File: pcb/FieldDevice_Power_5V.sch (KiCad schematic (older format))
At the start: 17 parts

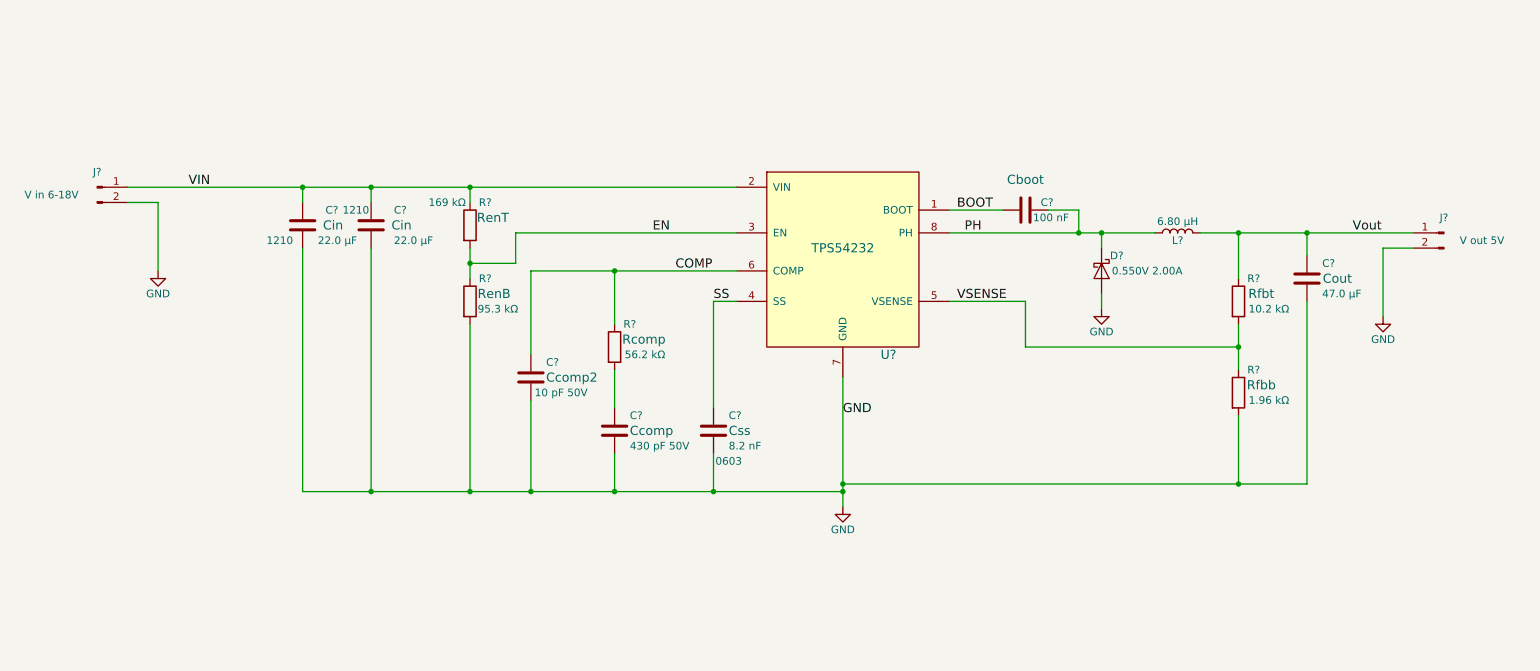
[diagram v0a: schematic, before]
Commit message: Completed the schematic and started the layout
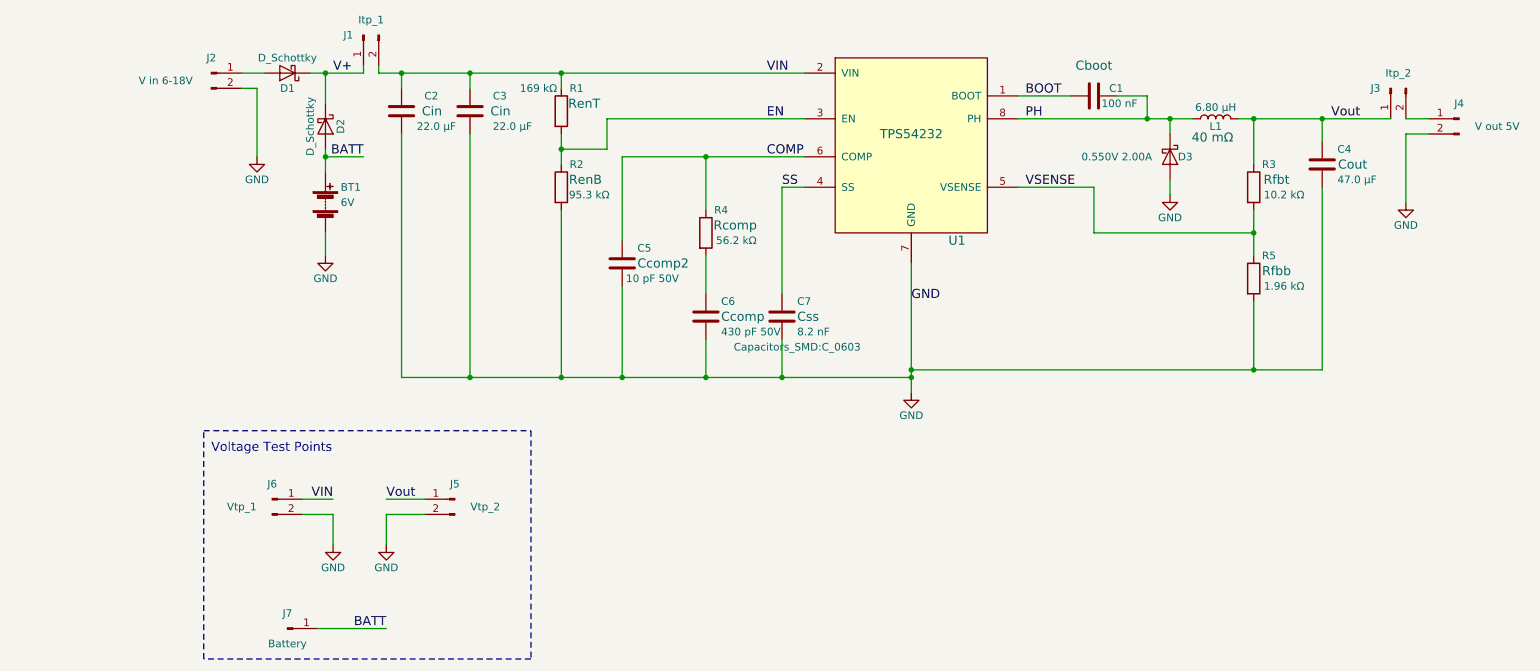
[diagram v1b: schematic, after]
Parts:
- added BT1: 6V, FieldDevice_Power_5V:BC4AAAPC_BATTERYHOLDER_4xAAA, symbol Battery
- added D1: D_Schottky, FieldDevice_Power_5V:B130-13-F, symbol D_Schottky
- added D2: D_Schottky, Diodes_SMD:D_SOD-123F, symbol D_Schottky
- added J1: Itp_1, Pin_Headers:Pin_Header_Straight_1x02_Pitch2.54mm, symbol Conn_01x02_Male
- added J3: Itp_2, Pin_Headers:Pin_Header_Straight_1x02_Pitch2.54mm, symbol Conn_01x02_Male
- added J5: Vtp_2, Pin_Headers:Pin_Header_Straight_1x02_Pitch2.54mm, symbol Conn_01x02_Male
- added J6: Vtp_1, Pin_Headers:Pin_Header_Straight_1x02_Pitch2.54mm, symbol Conn_01x02_Male
- added J7: Battery, Pin_Headers:Pin_Header_Straight_1x01, symbol Conn_01x01_Male
- C1, C4, C5, C6: renamed from C?; footprint (none) -> Capacitors_SMD:C_0805
- C2, C3: renamed from C?; footprint 1210 -> Capacitors_SMD:C_1210; ConradPN (none) -> Value; Label (none) -> Value; MPN (none) -> Value
- C7: renamed from C?; footprint 0603 -> Capacitors_SMD:C_0603
- D3: renamed from D?; footprint SOD-123F -> Diodes_SMD:D_SOD-123F; ConradPN (none) -> Value; Label (none) -> Value; MPN (none) -> SS24FL
- J2, J4: renamed from J?; footprint (none) -> Pin_Headers:Pin_Header_Straight_1x02_Pitch2.54mm
- L1: renamed from L?; footprint (none) -> FieldDevice_Power_5V:SDR0805-6R8ML; Comp_Name Value -> 40 mΩ; ConradPN (none) -> Value; Label (none) -> Value; MPN (none) -> Value
- R1, R2, R3, R4, R5: renamed from R?; footprint (none) -> Resistors_SMD:R_0805
- U1: renamed from U?; footprint (none) -> FieldDevice_Power_5V:TPS54232DR
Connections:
- net GND: now also BT1.2 (-), J5.2 (Pin_2), J6.2 (Pin_2)
- net VIN: now also J1.2 (Pin_2), J6.1 (Pin_1); no longer J2.1 (Pin_1)
- net Vout: now also J3.1 (Pin_1), J5.1 (Pin_1); no longer J4.1 (Pin_1)
- new net: J3.2 (Pin_2), J4.1 (Pin_1)
- new net: D1.2 (A), J2.1 (Pin_1)
- new net BATT: BT1.1 (+), D2.2 (A), J7.1 (Pin_1)
- new net V+: D1.1 (K), D2.1 (K), J1.1 (Pin_1)
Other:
- note added: "Voltage Test Points"
- moved on the sheet: C1, C2, C3, C4, C5, C6, C7, D3, J2, J4, L1, R1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

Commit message: More on the layout
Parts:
- D1: value D_Schottky -> B130-13-F
- D2: value D_Schottky -> B130-13-F; footprint Diodes_SMD:D_SOD-123F -> FieldDevice_Power_5V:B130-13-F
- D3: footprint Diodes_SMD:D_SOD-123F -> FieldDevice_Power_5V:D_SOD-123F
- J1, J2, J3, J4, J5, J6: footprint Pin_Headers:Pin_Header_Straight_1x02_Pitch2.54mm -> Pin_Headers:Pin_Header_Angled_1x02_Pitch2.54mm
- J7: footprint Pin_Headers:Pin_Header_Straight_1x01 -> Pin_Headers:Pin_Header_Angled_1x01
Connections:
- net GND: now also J6.1 (Pin_1); no longer J6.2 (Pin_2)
- net VIN: now also J6.2 (Pin_2); no longer J6.1 (Pin_1)
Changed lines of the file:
@@
 F 0 "D3" V 8250 2650 50  0000 C CNN
 F 1 "0.550V 2.00A" V 8250 2200 50  0000 C CNN
-F 2 "Diodes_SMD:D_SOD-123F" H 8250 2550 50  0001 C CNN
+F 2 "FieldDevice_Power_5V:D_SOD-123F" H 8250 2550 50  0001 C CNN
 F 3 "https://www.fairchildsemi.com/datasheets/SS/SS24FL.pdf" H 8250 2550 50  0001 C CNN
 F 4 "SS24FL" H 8250 2550 60  0001 C CNN "MPN"
@@
 F 0 "J4" H 10150 2400 50  0000 C CNN
 F 1 "V out 5V" H 9900 2250 50  0000 C CNN
-F 2 "Pin_Headers:Pin_Header_Straight_1x02_Pitch2.54mm" H 10150 2300 50  0001 C CNN
+F 2 "Pin_Headers:Pin_Header_Angled_1x02_Pitch2.54mm" H 10150 2300 50  0001 C CNN
 F 3 "" H 10150 2300 50  0001 C CNN
 F 4 "Value" H 10150 2300 60  0001 C CNN "Link"
@@
 F 0 "J2" H 1950 2100 50  0000 C CNN
 F 1 "V in 6-18V" H 1650 1950 50  0000 C CNN
-F 2 "Pin_Headers:Pin_Header_Straight_1x02_Pitch2.54mm" H 1950 2000 50  0001 C CNN
+F 2 "Pin_Headers:Pin_Header_Angled_1x02_Pitch2.54mm" H 1950 2000 50  0001 C CNN
 F 3 "" H 1950 2000 50  0001 C CNN
 F 4 "Value" H 1950 2000 60  0001 C CNN "Link"
@@
 F 0 "J1" V 2950 1850 50  0000 C CNN
 F 1 "Itp_1" V 2850 1700 50  0000 C CNN
-F 2 "Pin_Headers:Pin_Header_Straight_1x02_Pitch2.54mm" H 2950 1750 50  0001 C CNN
+F 2 "Pin_Headers:Pin_Header_Angled_1x02_Pitch2.54mm" H 2950 1750 50  0001 C CNN
 F 3 "" H 2950 1750 50  0001 C CNN
 F 4 "Value" H 2950 1750 60  0001 C CNN "Link"
@@
 F 0 "J3" V 9700 2200 50  0000 C CNN
 F 1 "Itp_2" V 9600 2050 50  0000 C CNN
-F 2 "Pin_Headers:Pin_Header_Straight_1x02_Pitch2.54mm" H 9700 2100 50  0001 C CNN
+F 2 "Pin_Headers:Pin_Header_Angled_1x02_Pitch2.54mm" H 9700 2100 50  0001 C CNN
 F 3 "" H 9700 2100 50  0001 C CNN
 F 4 "Value" H 9700 2100 60  0001 C CNN "Link"
@@
 F 0 "J5" H 3550 4900 50  0000 C CNN
 F 1 "Vtp_2" H 3350 4750 50  0000 C CNN
-F 2 "Pin_Headers:Pin_Header_Straight_1x02_Pitch2.54mm" H 3550 4800 50  0001 C CNN
+F 2 "Pin_Headers:Pin_Header_Angled_1x02_Pitch2.54mm" H 3550 4800 50  0001 C CNN
 F 3 "" H 3550 4800 50  0001 C CNN
 F 4 "Value" H 3550 4800 60  0001 C CNN "Link"
@@
 L Conn_01x02_Male J6
 U 1 1 5A480F50
-P 2350 4800
-F 0 "J6" H 2350 4900 50  0000 C CNN
-F 1 "Vtp_1" H 2150 4750 50  0000 C CNN
-F 2 "Pin_Headers:Pin_Header_Straight_1x02_Pitch2.54mm" H 2350 4800 50  0001 C CNN
-F 3 "" H 2350 4800 50  0001 C CNN
-F 4 "Value" H 2350 4800 60  0001 C CNN "Link"
-F 5 "V in 6-18V" H 2000 4750 60  0001 C CNN "Comp_Name"
-	1    2350 4800
-	1    0    0    -1
+P 2350 4900
+F 0 "J6" H 2350 5000 50  0000 C CNN
+F 1 "Vtp_1" H 2150 4850 50  0000 C CNN
+F 2 "Pin_Headers:Pin_Header_Angled_1x02_Pitch2.54mm" H 2350 4900 50  0001 C CNN
+F 3 "" H 2350 4900 50  0001 C CNN
+F 4 "Value" H 2350 4900 60  0001 C CNN "Link"
+F 5 "V in 6-18V" H 2000 4850 60  0001 C CNN "Comp_Name"
+	1    2350 4900
+	1    0    0    1
 $EndComp
 Wire Wire Line
@@
 P 2450 2000
 F 0 "D1" H 2450 2100 50  0000 C CNN
-F 1 "D_Schottky" H 2450 1900 50  0000 C CNN
+F 1 "B130-13-F" H 2450 1900 50  0000 C CNN
 F 2 "FieldDevice_Power_5V:B130-13-F" H 2450 2000 50  0001 C CNN
 F 3 "" H 2450 2000 50  0001 C CNN
@@
 P 2700 2350
 F 0 "D2" H 2700 2450 50  0000 C CNN
-F 1 "D_Schottky" H 2700 2250 50  0000 C CNN
-F 2 "Diodes_SMD:D_SOD-123F" H 2700 2350 50  0001 C CNN
+F 1 "B130-13-F" H 2700 2250 50  0000 C CNN
+F 2 "FieldDevice_Power_5V:B130-13-F" H 2700 2350 50  0001 C CNN
 F 3 "" H 2700 2350 50  0001 C CNN
 F 4 "B130-13-F" H 2700 2350 60  0001 C CNN "MPN"
@@
 F 0 "J7" H 2450 5750 50  0000 C CNN
 F 1 "Battery" H 2450 5550 50  0000 C CNN
-F 2 "Pin_Headers:Pin_Header_Straight_1x01" H 2450 5650 50  0001 C CNN
+F 2 "Pin_Headers:Pin_Header_Angled_1x01" H 2450 5650 50  0001 C CNN
 F 3 "" H 2450 5650 50  0001 C CNN
 	1    2450 5650

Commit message: Finishing up the layout
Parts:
- J1, J3, J5, J6: footprint Pin_Headers:Pin_Header_Angled_1x02_Pitch2.54mm -> Pin_Headers:Pin_Header_Straight_1x02_Pitch2.54mm
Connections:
- net V5+: now reaches J3.2 (Pin_2), J4.1 (Pin_1)
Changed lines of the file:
@@
 F 0 "J1" V 2950 1850 50  0000 C CNN
 F 1 "Itp_1" V 2850 1700 50  0000 C CNN
-F 2 "Pin_Headers:Pin_Header_Angled_1x02_Pitch2.54mm" H 2950 1750 50  0001 C CNN
+F 2 "Pin_Headers:Pin_Header_Straight_1x02_Pitch2.54mm" H 2950 1750 50  0001 C CNN
 F 3 "" H 2950 1750 50  0001 C CNN
 F 4 "Value" H 2950 1750 60  0001 C CNN "Link"
@@
 F 0 "J3" V 9700 2200 50  0000 C CNN
 F 1 "Itp_2" V 9600 2050 50  0000 C CNN
-F 2 "Pin_Headers:Pin_Header_Angled_1x02_Pitch2.54mm" H 9700 2100 50  0001 C CNN
+F 2 "Pin_Headers:Pin_Header_Straight_1x02_Pitch2.54mm" H 9700 2100 50  0001 C CNN
 F 3 "" H 9700 2100 50  0001 C CNN
 F 4 "Value" H 9700 2100 60  0001 C CNN "Link"
@@
 F 0 "J5" H 3550 4900 50  0000 C CNN
 F 1 "Vtp_2" H 3350 4750 50  0000 C CNN
-F 2 "Pin_Headers:Pin_Header_Angled_1x02_Pitch2.54mm" H 3550 4800 50  0001 C CNN
+F 2 "Pin_Headers:Pin_Header_Straight_1x02_Pitch2.54mm" H 3550 4800 50  0001 C CNN
 F 3 "" H 3550 4800 50  0001 C CNN
 F 4 "Value" H 3550 4800 60  0001 C CNN "Link"
@@
 F 0 "J6" H 2350 5000 50  0000 C CNN
 F 1 "Vtp_1" H 2150 4850 50  0000 C CNN
-F 2 "Pin_Headers:Pin_Header_Angled_1x02_Pitch2.54mm" H 2350 4900 50  0001 C CNN
+F 2 "Pin_Headers:Pin_Header_Straight_1x02_Pitch2.54mm" H 2350 4900 50  0001 C CNN
 F 3 "" H 2350 4900 50  0001 C CNN
 F 4 "Value" H 2350 4900 60  0001 C CNN "Link"
@@
 Wire Notes Line
 	1900 5850 1900 4350
+Text Label 9850 2300 0    60   ~ 0
+V5+
 $EndSCHEMATC

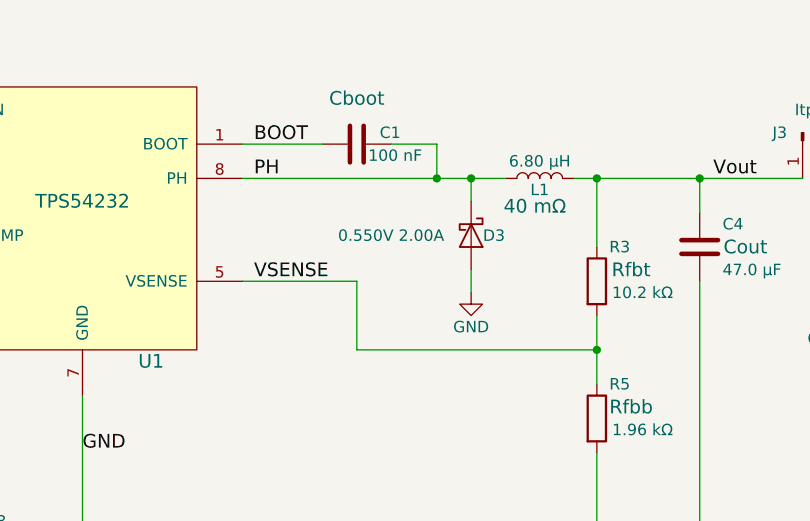
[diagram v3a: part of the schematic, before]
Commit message: Correct to C4 footprint
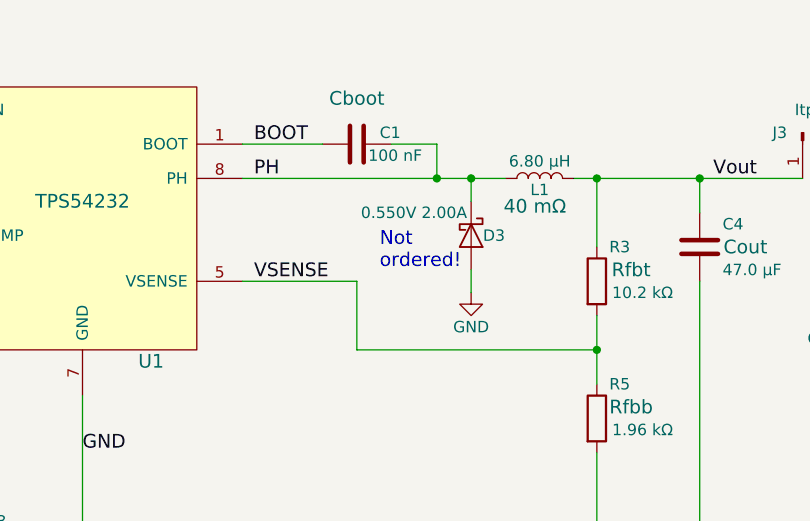
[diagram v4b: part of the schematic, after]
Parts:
- C4: footprint Capacitors_SMD:C_0805 -> Capacitors_SMD:C_1210
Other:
- note added: "Not \nordered!"
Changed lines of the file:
@@
 F 0 "C4" H 9350 2700 50  0000 L CNN
 F 1 "47.0 μF" H 9350 2500 50  0000 L CNN
-F 2 "Capacitors_SMD:C_0805" H 9288 2450 50  0001 C CNN
+F 2 "Capacitors_SMD:C_1210" H 9288 2450 50  0001 C CNN
 F 3 "" H 9250 2600 50  0001 C CNN
 F 4 "Value" H 9250 2600 60  0001 C CNN "Link"
@@
 P 8250 2550
 F 0 "D3" V 8250 2650 50  0000 C CNN
-F 1 "0.550V 2.00A" V 8250 2200 50  0000 C CNN
+F 1 "0.550V 2.00A" V 8150 2300 50  0000 C CNN
 F 2 "FieldDevice_Power_5V:D_SOD-123F" H 8250 2550 50  0001 C CNN
 F 3 "https://www.fairchildsemi.com/datasheets/SS/SS24FL.pdf" H 8250 2550 50  0001 C CNN
 F 4 "SS24FL" H 8250 2550 60  0001 C CNN "MPN"
-F 5 "Value" H 8250 2550 60  0001 C CNN "ConradPN"
-F 6 "Value" H 8250 2550 60  0001 C CNN "Label"
-F 7 "Value" H 8250 2550 60  0001 C CNN "Link"
-F 8 "Value" H 8250 2550 60  0001 C CNN "Comp_Name"
+F 5 "Value" H 8250 2550 60  0001 C CNN "Link"
+F 6 "Value" H 8250 2550 60  0001 C CNN "Comp_Name"
+F 7 "Value" H 8250 2550 60  0001 C CNN "ConradPN"
+F 8 "Value" H 8250 2550 60  0001 C CNN "Label"
 	1    8250 2550
 	0    1    1    0
@@
 Text Label 9850 2300 0    60   ~ 0
 V5+
+Text Notes 7850 2700 0    60   ~ 0
+Not \nordered!
 $EndSCHEMATC

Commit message: Changed the footprint for C4
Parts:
- C4: footprint Capacitors_SMD:C_1210 -> Capacitors_SMD:C_1206
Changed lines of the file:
@@
 F 0 "C4" H 9350 2700 50  0000 L CNN
 F 1 "47.0 μF" H 9350 2500 50  0000 L CNN
-F 2 "Capacitors_SMD:C_1210" H 9288 2450 50  0001 C CNN
+F 2 "Capacitors_SMD:C_1206" H 9288 2450 50  0001 C CNN
 F 3 "" H 9250 2600 50  0001 C CNN
 F 4 "Value" H 9250 2600 60  0001 C CNN "Link"
